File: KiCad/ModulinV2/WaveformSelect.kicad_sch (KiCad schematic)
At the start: 54 parts, among them IC10 SN74AHC1G02DBVR, IC11 SN74AHCT1G00DBVR, IC12 SN74AHCT1G00DBVR, IC13 SN74AHC1G02DBVR, IC14 SN74AHCT1G00DBVR, IC15 SN74AHC1G08DBVR, IC16 SN74HC193DR, IC17 TMUX4052DYYR, IC18 TMUX4051DYYRQ1, IC19 TMUX4051DYYRQ1, IC9 NC7SZ74K8X, J6 TSW-104-07-T-D, J7 TSW-104-07-T-D, J8 TSW-104-07-T-D, J9 TSW-104-07-T-D

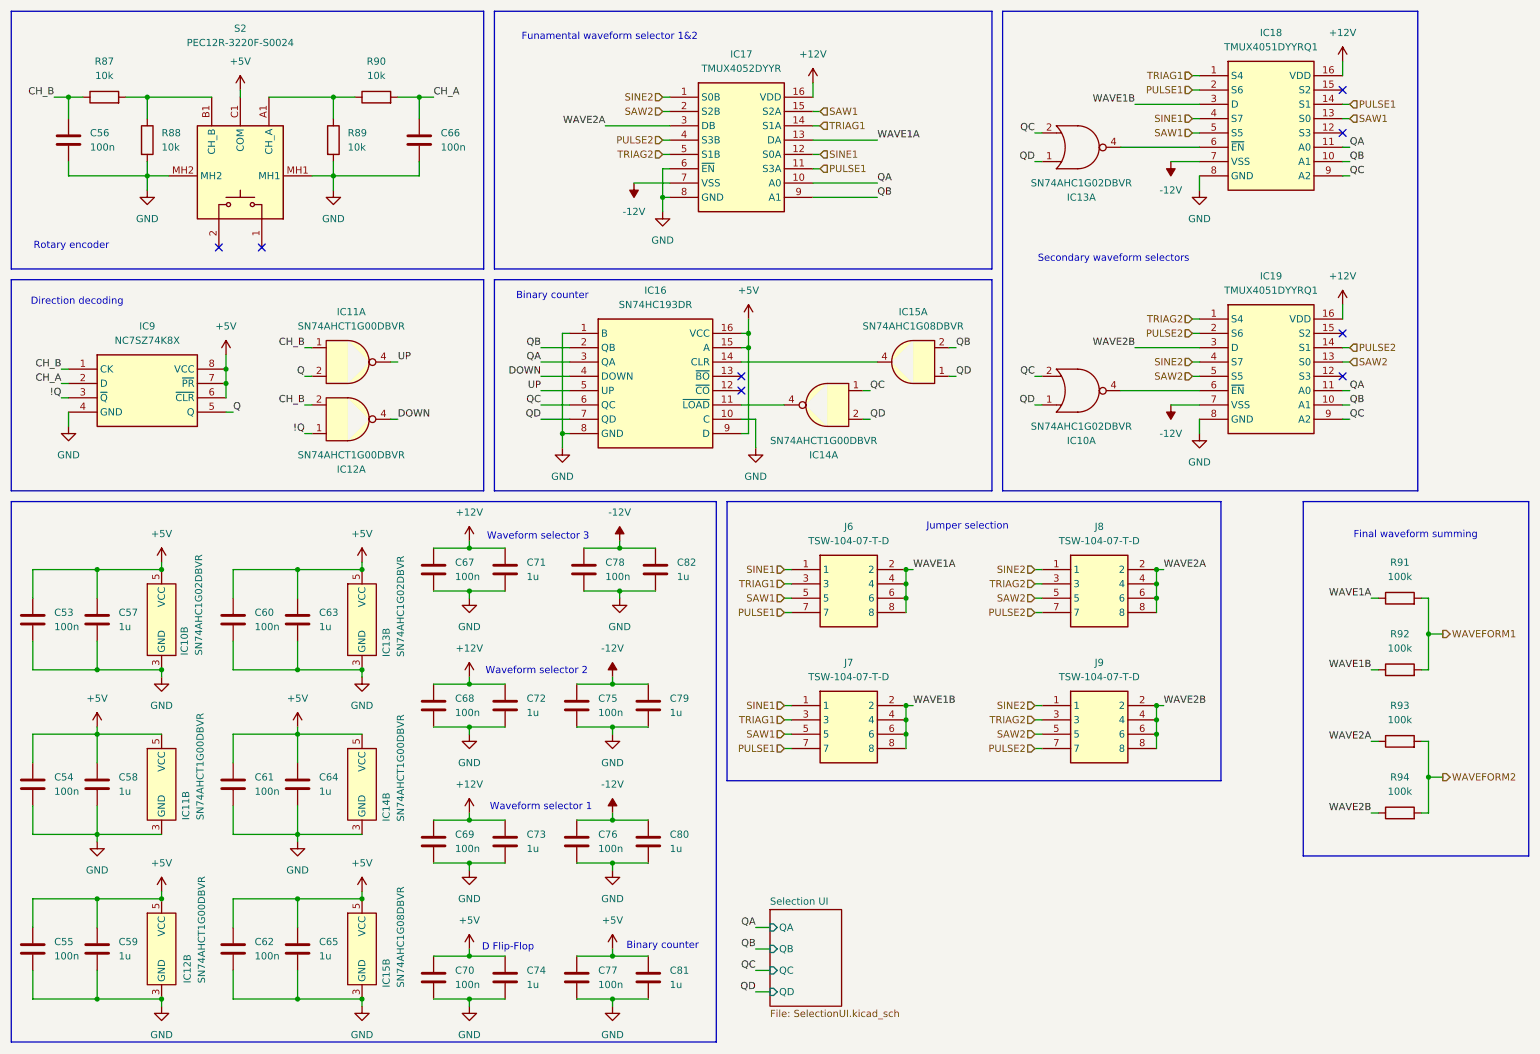
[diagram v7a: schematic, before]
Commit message: Fixed library issues and assigned most footprints
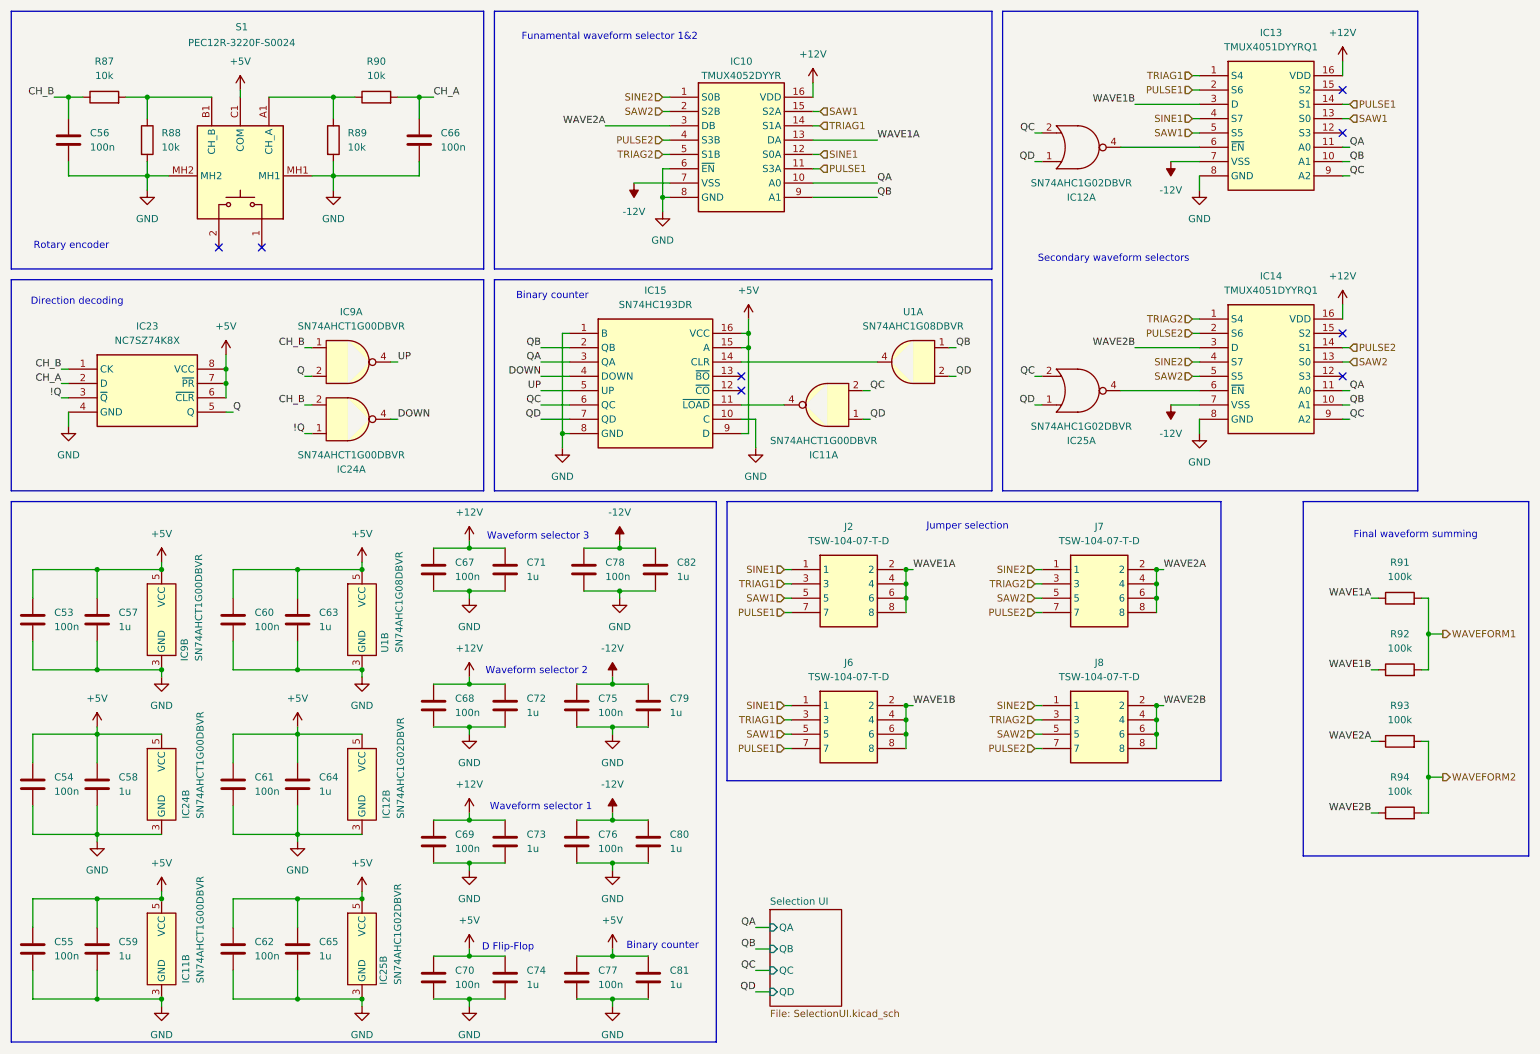
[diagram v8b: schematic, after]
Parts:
- removed IC10, IC13: SN74AHC1G02DBVR, symbol SN74AHC1G02DBVR:SN74AHC1G02DBVR_Alt
- removed IC11, IC12, IC14: SN74AHCT1G00DBVR, symbol SN74AHCT1G00DBVR:SN74AHCT1G00DBVR_Alt
- removed IC15: SN74AHC1G08DBVR, symbol SN74AHC1G08DBVR:SN74AHC1G08DBVR_Alt
- removed IC16: SN74HC193DR, SOIC127P600X175-16N, symbol SN74HC193DR:SN74HC193DR
- removed IC17: TMUX4052DYYR, SOP50P326X110-16N, symbol TMUX4052DYYR:TMUX4052DYYR
- removed IC18, IC19: TMUX4051DYYRQ1, SOP50P326X110-16N, symbol TMUX4051DYYRQ1:TMUX4051DYYRQ1
- removed IC9: NC7SZ74K8X, SOP50P310X90-8N, symbol NC7SZ74K8X:NC7SZ74K8X
- removed J6, J7, J8, J9: TSW-104-07-T-D, TSW-104-XX-YY-D, symbol TSW-104-07-T-D:TSW-104-07-T-D
- removed S2: PEC12R-3220F-S0024, PEC12R3220FS0024, symbol PEC12R-3220F-S0024:PEC12R-3220F-S0024
- added IC10: TMUX4052DYYR, SamacSys_Parts:SOP50P326X110-16N, symbol SamacSys_Parts:TMUX4052DYYR
- added IC11, IC24, IC9: SN74AHCT1G00DBVR, SamacSys_Parts:SOT95P280X145-5N, symbol SamacSys_Parts:SN74AHCT1G00DBVR
- added IC12, IC25: SN74AHC1G02DBVR, SamacSys_Parts:SOT95P280X145-5N, symbol SamacSys_Parts:SN74AHC1G02DBVR
- added IC13, IC14: TMUX4051DYYRQ1, SamacSys_Parts:SOP50P326X110-16N, symbol SamacSys_Parts:TMUX4051DYYRQ1
- added IC15: SN74HC193DR, SamacSys_Parts:SOIC127P600X175-16N, symbol SamacSys_Parts:SN74HC193DR
- added IC23: NC7SZ74K8X, SamacSys_Parts:SOP50P310X90-8N, symbol SamacSys_Parts:NC7SZ74K8X
- added J2, J6, J7, J8: TSW-104-07-T-D, SamacSys_Parts:TSW-104-XX-YY-D, symbol SamacSys_Parts:TSW-104-07-T-D
- added S1: PEC12R-3220F-S0024, SamacSys_Parts:PEC12R3220FS0024, symbol SamacSys_Parts:PEC12R-3220F-S0024
- added U1: SN74AHC1G08DBVR, SamacSys_Parts:SOT95P280X145-5N, symbol SamacSys_Parts:SN74AHC1G08DBVR
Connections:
- net !Q: now also IC23.3 (~{Q}), IC24.1
- net +12V: now also IC10.16 (VDD), IC13.16 (VDD), IC14.16 (VDD)
- net +5V: now also IC11.5 (VCC), IC12.5 (VCC), IC15.15 (A), IC15.16 (VCC), IC15.9 (D), IC23.6 (~{CLR}), IC23.7 (~{PR}), IC23.8 (VCC), IC24.5 (VCC), IC25.5 (VCC), IC9.5 (VCC), S1.C1 (COM), U1.5 (VCC)
- net -12V: now also IC10.7 (VSS), IC13.7 (VSS), IC14.7 (VSS)
- net CH_A: now also IC23.2 (D)
- net CH_B: now also IC23.1 (CK), IC24.2, IC9.1
- net DOWN: now also IC15.4 (DOWN), IC24.4
- net GND: now also IC10.6 (~{EN}), IC10.8 (GND), IC11.3 (GND), IC12.3 (GND), IC13.8 (GND), IC14.8 (GND), IC15.1 (B), IC15.10 (C), IC15.8 (GND), IC23.4 (GND), IC24.3 (GND), IC25.3 (GND), IC9.3 (GND), S1.MH1, S1.MH2, U1.3 (GND)
- net PULSE1: now also IC10.11 (S3A), IC13.14 (S1), IC13.2 (S6), J2.7, J6.7
- net PULSE2: now also IC10.4 (S3B), IC14.14 (S1), IC14.2 (S6), J7.7, J8.7
- net Q: now also IC23.5 (Q), IC9.2
- net QA: now also IC10.10 (A0), IC13.11 (A0), IC14.11 (A0), IC15.3 (QA)
- net QB: now also IC10.9 (A1), IC13.10 (A1), IC14.10 (A1), IC15.2 (QB), U1.1
- net QC: now also IC11.2, IC12.2, IC13.9 (A2), IC14.9 (A2), IC15.6 (QC), IC25.2
- net QD: now also IC11.1, IC12.1, IC15.7 (QD), IC25.1, U1.2
- net SAW1: now also IC10.15 (S2A), IC13.13 (S0), IC13.5 (S5), J2.5, J6.5
- net SAW2: now also IC10.2 (S2B), IC14.13 (S0), IC14.5 (S5), J7.5, J8.5
- net SINE1: now also IC10.12 (S0A), IC13.4 (S7), J2.1, J6.1
- net SINE2: now also IC10.1 (S0B), IC14.4 (S7), J7.1, J8.1
- net TRIAG1: now also IC10.14 (S1A), IC13.1 (S4), J2.3, J6.3
- net TRIAG2: now also IC10.5 (S1B), IC14.1 (S4), J7.3, J8.3
- net UP: now also IC15.5 (UP), IC9.4
- net WAVE1A: now also IC10.13 (DA), J2.2, J2.4, J2.6, J2.8
- net WAVE1B: now also IC13.3 (D), J6.2, J6.4, J6.6, J6.8
- net WAVE2A: now also IC10.3 (DB), J7.2, J7.4, J7.6, J7.8
- net WAVE2B: now also IC14.3 (D), J8.2, J8.4, J8.6, J8.8
- net at R87.2, R88.1: now also S1.B1 (CH_B)
- net at R89.1, R90.1: now also S1.A1 (CH_A)
- new net: IC12.4, IC13.6 (~{EN})
- new net: IC11.4, IC15.11 (~{LOAD})
- new net: IC15.14 (CLR), U1.4
- new net: IC14.6 (~{EN}), IC25.4
